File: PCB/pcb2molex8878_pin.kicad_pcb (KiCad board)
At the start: 2 copper layers, 16 x 38.2 mm, 2 parts

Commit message: fix pocket dims to account for fitment clearance
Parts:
- gave numbers to parts that had none: 1
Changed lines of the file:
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@@
     (descr "Castellated edge contacts to fit Molex 8878 Socket")
     (solder_mask_margin -0.28)
-    (fp_text reference J? (at -0.9906 -0.9906 -90) (layer Dwgs.User) hide
+    (fp_text reference m? (at -0.9906 -0.9906 -90) (layer Dwgs.User) hide
       (effects (font (size 1.2065 1.2065) (thickness 0.127)) (justify left bottom))
     )
@@
       (effects (font (size 1.2065 1.2065) (thickness 0.1016)) (justify left bottom))
     )
+    (fp_line (start 7.2 18.3) (end -7.2 18.3) (layer Dwgs.User) (width 0.01))
+    (fp_line (start 7.2 -18.3) (end 7.2 18.3) (layer Dwgs.User) (width 0.01))
+    (fp_line (start -7.2 -18.3) (end 7.2 -18.3) (layer Dwgs.User) (width 0.01))
+    (fp_line (start -7.2 18.3) (end -7.2 -18.3) (layer Dwgs.User) (width 0.01))
     (fp_text user "backside components" (at -4.4 2.15) (layer Dwgs.User)
       (effects (font (size 0.2 0.2) (thickness 0.01)))
     )
-    (fp_text user "36.7 x 14.5 x 1.6 pocket" (at -4.4 1.85) (layer Dwgs.User)
+    (fp_text user "36.6 x 14.4 x 1.6 pocket" (at -4.4 1.85) (layer Dwgs.User)
       (effects (font (size 0.2 0.2) (thickness 0.01)))
     )
-    (fp_line (start -7.25 2) (end -6.5 2) (layer Dwgs.User) (width 0.01))
-    (fp_line (start -7.25 2) (end -7 2.25) (layer Dwgs.User) (width 0.01))
-    (fp_line (start -7.25 2) (end -7 1.75) (layer Dwgs.User) (width 0.01))
-    (fp_line (start -7.25 18.35) (end -7.25 -18.35) (layer Dwgs.User) (width 0.01))
-    (fp_line (start 7.25 18.35) (end -7.25 18.35) (layer Dwgs.User) (width 0.01))
-    (fp_line (start 7.25 -18.35) (end 7.25 18.35) (layer Dwgs.User) (width 0.01))
-    (fp_line (start -7.25 -18.35) (end 7.25 -18.35) (layer Dwgs.User) (width 0.01))
+    (fp_line (start -7.2 2) (end -6.45 2) (layer Dwgs.User) (width 0.01))
+    (fp_line (start -7.2 2) (end -6.95 2.25) (layer Dwgs.User) (width 0.01))
+    (fp_line (start -7.2 2) (end -6.95 1.75) (layer Dwgs.User) (width 0.01))
     (fp_line (start -8 -19.1) (end 8 -19.1) (layer Eco2.User) (width 0.01))
     (fp_line (start 8 19.1) (end 8 -19.1) (layer Eco2.User) (width 0.01))

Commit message: show retainer wedges on pcb drawings. add daughterboard in carrier model.
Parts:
- gave numbers to parts that had none: 2
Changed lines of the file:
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@@
     (descr "Castellated edge contacts to fit Molex 8878 Socket")
     (solder_mask_margin -0.28)
-    (fp_text reference m? (at -0.9906 -0.9906 -90) (layer Dwgs.User) hide
+    (fp_text reference carrier1 (at -0.9906 -0.9906 -90) (layer Dwgs.User) hide
       (effects (font (size 1.2065 1.2065) (thickness 0.127)) (justify left bottom))
     )
@@
       (effects (font (size 1.2065 1.2065) (thickness 0.1016)) (justify left bottom))
     )
+    (fp_text user "10.0 x 1.0 retainer wedges on top surface" (at 0.5 -17.1) (layer Dwgs.User)
+      (effects (font (size 0.2 0.2) (thickness 0.01)))
+    )
+    (fp_line (start -3 -18.1) (end -2.8 -17.9) (layer Dwgs.User) (width 0.01))
+    (fp_line (start -3 -18.1) (end -3.2 -17.9) (layer Dwgs.User) (width 0.01))
+    (fp_line (start -3 -18.1) (end -3 -17) (layer Dwgs.User) (width 0.01))
+    (fp_line (start 5 19.1) (end -5 19.1) (layer Dwgs.User) (width 0.01))
+    (fp_line (start 5 18.1) (end 5 19.1) (layer Dwgs.User) (width 0.01))
+    (fp_line (start -5 18.1) (end 5 18.1) (layer Dwgs.User) (width 0.01))
+    (fp_line (start -5 19.1) (end -5 18.1) (layer Dwgs.User) (width 0.01))
+    (fp_line (start 5 -19.1) (end -5 -19.1) (layer Dwgs.User) (width 0.01))
+    (fp_line (start 5 -18.1) (end 5 -19.1) (layer Dwgs.User) (width 0.01))
+    (fp_line (start -5 -18.1) (end 5 -18.1) (layer Dwgs.User) (width 0.01))
+    (fp_line (start -5 -19.1) (end -5 -18.1) (layer Dwgs.User) (width 0.01))
     (fp_line (start 7.2 18.3) (end -7.2 18.3) (layer Dwgs.User) (width 0.01))
     (fp_line (start 7.2 -18.3) (end 7.2 18.3) (layer Dwgs.User) (width 0.01))
@@
     (descr "Castellated edge contacts to fit Molex 8878 Socket")
     (solder_mask_margin -0.28)
-    (fp_text reference J? (at -0.9906 -0.9906 -90) (layer Dwgs.User) hide
+    (fp_text reference contacts1 (at -0.9906 -0.9906 -90) (layer Dwgs.User) hide
       (effects (font (size 1.2065 1.2065) (thickness 0.127)) (justify left bottom))
     )

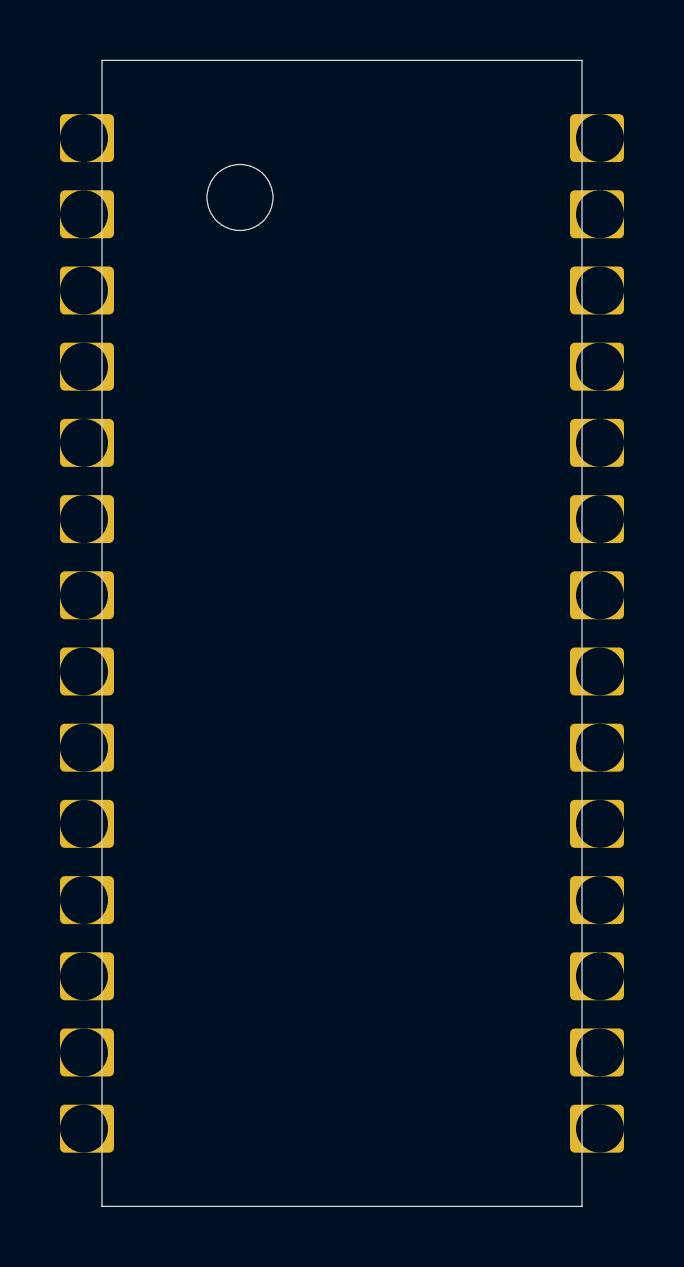
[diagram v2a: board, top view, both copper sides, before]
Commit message: update 'pin' variant with new dims
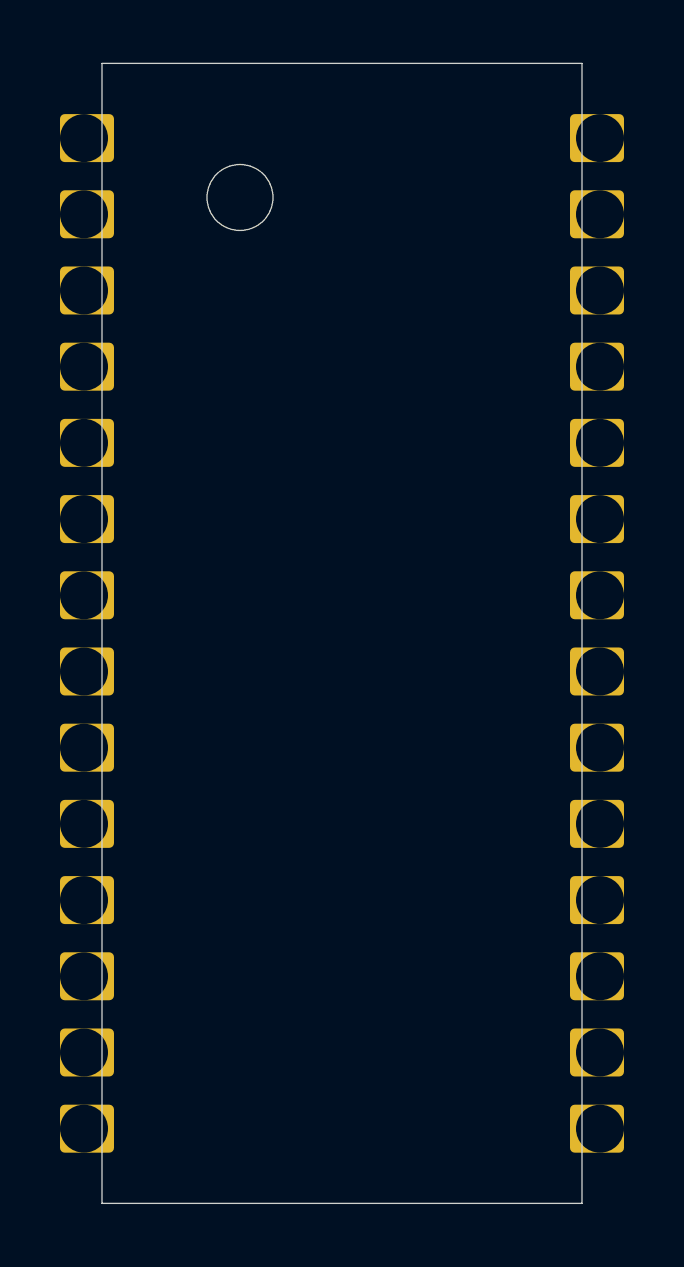
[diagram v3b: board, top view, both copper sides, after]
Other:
- board size 16 x 38.2 mm -> 16 x 38 mm
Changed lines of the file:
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@@
-(kicad_pcb (version 20171130) (host pcbnew 5.1.4-e60b266~84~ubuntu19.04.1)
+(kicad_pcb (version 20171130) (host pcbnew 5.1.5-52549c5~84~ubuntu19.04.1)
   (general
     (thickness 1.6)
@@
       (effects (font (size 1.2065 1.2065) (thickness 0.1016)) (justify left bottom))
     )
-    (fp_text user "10.0 x 1.0 retainer wedges on top surface" (at 0.5 -17.1) (layer Dwgs.User)
-      (effects (font (size 0.2 0.2) (thickness 0.01)))
-    )
-    (fp_line (start -3 -18.1) (end -2.8 -17.9) (layer Dwgs.User) (width 0.01))
-    (fp_line (start -3 -18.1) (end -3.2 -17.9) (layer Dwgs.User) (width 0.01))
-    (fp_line (start -3 -18.1) (end -3 -17) (layer Dwgs.User) (width 0.01))
-    (fp_line (start 5 19.1) (end -5 19.1) (layer Dwgs.User) (width 0.01))
-    (fp_line (start 5 18.1) (end 5 19.1) (layer Dwgs.User) (width 0.01))
-    (fp_line (start -5 18.1) (end 5 18.1) (layer Dwgs.User) (width 0.01))
-    (fp_line (start -5 19.1) (end -5 18.1) (layer Dwgs.User) (width 0.01))
-    (fp_line (start 5 -19.1) (end -5 -19.1) (layer Dwgs.User) (width 0.01))
-    (fp_line (start 5 -18.1) (end 5 -19.1) (layer Dwgs.User) (width 0.01))
-    (fp_line (start -5 -18.1) (end 5 -18.1) (layer Dwgs.User) (width 0.01))
-    (fp_line (start -5 -19.1) (end -5 -18.1) (layer Dwgs.User) (width 0.01))
+    (fp_line (start -6.14 -16.78) (end -5.17 -16.78) (layer Dwgs.User) (width 0.01))
+    (fp_line (start -6.14 -18.3) (end -6.14 -16.78) (layer Dwgs.User) (width 0.01))
+    (fp_line (start -3.82 -17.45) (end -3.03 -17.45) (layer Dwgs.User) (width 0.01))
+    (fp_line (start -3.82 -18) (end -3.82 -17.45) (layer Dwgs.User) (width 0.01))
+    (fp_line (start -6.14 -18.3) (end -5.94 -18.1) (layer Dwgs.User) (width 0.01))
+    (fp_line (start -6.14 -18.3) (end -6.34 -18.1) (layer Dwgs.User) (width 0.01))
+    (fp_text user "10.0 x 1.0 retainer wedges on top surface" (at 0.3 -17.44) (layer Dwgs.User)
+      (effects (font (size 0.2 0.2) (thickness 0.01)))
+    )
+    (fp_line (start -3.82 -18) (end -3.62 -17.8) (layer Dwgs.User) (width 0.01))
+    (fp_line (start -3.82 -18) (end -4.02 -17.8) (layer Dwgs.User) (width 0.01))
+    (fp_line (start 5 19) (end -5 19) (layer Dwgs.User) (width 0.01))
+    (fp_line (start 5 18) (end 5 19) (layer Dwgs.User) (width 0.01))
+    (fp_line (start -5 18) (end 5 18) (layer Dwgs.User) (width 0.01))
+    (fp_line (start -5 19) (end -5 18) (layer Dwgs.User) (width 0.01))
+    (fp_line (start 5 -19) (end -5 -19) (layer Dwgs.User) (width 0.01))
+    (fp_line (start 5 -18) (end 5 -19) (layer Dwgs.User) (width 0.01))
+    (fp_line (start -5 -18) (end 5 -18) (layer Dwgs.User) (width 0.01))
+    (fp_line (start -5 -19) (end -5 -18) (layer Dwgs.User) (width 0.01))
     (fp_line (start 7.2 18.3) (end -7.2 18.3) (layer Dwgs.User) (width 0.01))
     (fp_line (start 7.2 -18.3) (end 7.2 18.3) (layer Dwgs.User) (width 0.01))
     (fp_line (start -7.2 -18.3) (end 7.2 -18.3) (layer Dwgs.User) (width 0.01))
     (fp_line (start -7.2 18.3) (end -7.2 -18.3) (layer Dwgs.User) (width 0.01))
-    (fp_text user "backside components" (at -4.4 2.15) (layer Dwgs.User)
-      (effects (font (size 0.2 0.2) (thickness 0.01)))
-    )
-    (fp_text user "36.6 x 14.4 x 1.6 pocket" (at -4.4 1.85) (layer Dwgs.User)
-      (effects (font (size 0.2 0.2) (thickness 0.01)))
-    )
-    (fp_line (start -7.2 2) (end -6.45 2) (layer Dwgs.User) (width 0.01))
-    (fp_line (start -7.2 2) (end -6.95 2.25) (layer Dwgs.User) (width 0.01))
-    (fp_line (start -7.2 2) (end -6.95 1.75) (layer Dwgs.User) (width 0.01))
-    (fp_line (start -8 -19.1) (end 8 -19.1) (layer Eco2.User) (width 0.01))
-    (fp_line (start 8 19.1) (end 8 -19.1) (layer Eco2.User) (width 0.01))
-    (fp_line (start -8 -19.1) (end -8 19.1) (layer Eco2.User) (width 0.01))
-    (fp_line (start 8 19.1) (end -8 19.1) (layer Eco2.User) (width 0.01))
-    (fp_line (start -8 -19.1) (end 8 19.1) (layer Dwgs.User) (width 0.01))
-    (fp_line (start -8 19.1) (end 8 -19.1) (layer Dwgs.User) (width 0.01))
+    (fp_text user "36.6 x 14.4 x 1.6 - backside pocket" (at -2.24 -16.77) (layer Dwgs.User)
+      (effects (font (size 0.2 0.2) (thickness 0.01)))
+    )
+    (fp_line (start -8 -19) (end 8 -19) (layer Eco2.User) (width 0.01))
+    (fp_line (start 8 19) (end 8 -19) (layer Eco2.User) (width 0.01))
+    (fp_line (start -8 -19) (end -8 19) (layer Eco2.User) (width 0.01))
+    (fp_line (start 8 19) (end -8 19) (layer Eco2.User) (width 0.01))
     (fp_text user "Eco2.User is Edge.Cuts for use with \"pcb2molex8878_pin\" carrier." (at -0.05 13.65) (layer Eco2.User)
       (effects (font (size 0.2 0.2) (thickness 0.01)))
     )
-    (pad "" np_thru_hole circle (at -3.4 -14.53) (size 2.2 2.2) (drill 2.2) (layers *.Cu))
+    (pad "" np_thru_hole circle (at -3.4 -14.53) (size 2.2 2.2) (drill 2.2) (layers *.Cu *.Mask))
     (model ${KIPRJMOD}/000_LOCAL.pretty/3d/pcb2molex8878_pin.step
       (offset (xyz 0 0 -0.4))
@@
       (solder_mask_margin -0.19))
   )
-  (gr_line (start 139.2184 80.087) (end 155.2184 80.087) (layer Edge.Cuts) (width 0.0254))
-  (gr_line (start 139.2184 118.287) (end 139.2184 80.087) (layer Edge.Cuts) (width 0.0254))
-  (gr_line (start 155.2184 118.287) (end 155.2184 80.087) (layer Edge.Cuts) (width 0.0254))
-  (gr_line (start 139.2184 118.287) (end 155.2184 118.287) (layer Edge.Cuts) (width 0.0254))
+  (gr_line (start 155.2184 80.187) (end 155.2184 118.187) (layer Edge.Cuts) (width 0.0254))
+  (gr_line (start 139.2184 118.187) (end 139.2184 80.187) (layer Edge.Cuts) (width 0.0254))
+  (gr_line (start 139.2184 80.187) (end 155.2184 80.187) (layer Edge.Cuts) (width 0.0254))
+  (gr_line (start 139.2184 118.187) (end 155.2184 118.187) (layer Edge.Cuts) (width 0.0254))
 )
